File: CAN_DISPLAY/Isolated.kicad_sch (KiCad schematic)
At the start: 37 parts, among them J4 43-01199, J5 NMEA0183 Output, J7 NMEA0183 Input, J8 DCDC 5V, U3 ISO1050DUB, U4 AMS1117-5.0, U5 ISO3080DW

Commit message: Added Light Sensor
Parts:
- removed J5: NMEA0183 Output, TerminalBlock:TerminalBlock_Altech_AK300-3_P5.00mm, symbol Connector_Generic:Conn_01x03
- removed J7: NMEA0183 Input, TerminalBlock:TerminalBlock_Altech_AK300-3_P5.00mm, symbol Connector_Generic:Conn_01x03
- added J20: NMEA0183, TerminalBlock_Altech:Altech_AK300_1x06_P5.00mm_45-Degree, symbol Connector_Generic:Conn_01x06
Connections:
- net NMEA IN+: now also J20.3 (Pin_3)
- net NMEA IN-: now also J20.2 (Pin_2)
- net NMEA OUT+: now also J20.6 (Pin_6)
- net NMEA OUT-: now also J20.5 (Pin_5)
- net at JP1.1 (A): now also J20.1 (Pin_1), J20.4 (Pin_4)
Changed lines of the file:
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@@
   (junction (at 214.63 34.29) (diameter 0) (color 0 0 0 0)
   )
+  (junction (at 251.46 140.97) (diameter 0) (color 0 0 0 0)
+  )
   (junction (at 158.75 113.03) (diameter 0) (color 0 0 0 0)
   )
@@
   (junction (at 176.53 29.21) (diameter 0) (color 0 0 0 0)
   )
-  (junction (at 251.46 147.32) (diameter 0) (color 0 0 0 0)
-  )
   (junction (at 184.15 124.46) (diameter 0) (color 0 0 0 0)
   )
@@
     (stroke (width 0) (type default))
   )
+  (wire (pts (xy 246.38 135.89) (xy 254 135.89))
+    (stroke (width 0) (type default))
+  )
   (wire (pts (xy 194.31 34.29) (xy 196.85 34.29))
     (stroke (width 0) (type default))
@@
     (stroke (width 0) (type default))
   )
-  (wire (pts (xy 251.46 147.32) (xy 254 147.32))
-    (stroke (width 0) (type default))
-  )
   (wire (pts (xy 243.84 115.57) (xy 245.11 115.57))
     (stroke (width 0) (type default))
@@
     (stroke (width 0) (type default))
   )
-  (wire (pts (xy 251.46 147.32) (xy 251.46 156.21))
+  (wire (pts (xy 251.46 133.35) (xy 251.46 140.97))
     (stroke (width 0) (type default))
   )
@@
     (stroke (width 0) (type default))
   )
-  (wire (pts (xy 243.84 138.43) (xy 243.84 142.24))
-    (stroke (width 0) (type default))
-  )
   (wire (pts (xy 176.53 64.77) (xy 158.75 64.77))
     (stroke (width 0) (type default))
@@
     (stroke (width 0) (type default))
   )
+  (wire (pts (xy 248.92 140.97) (xy 248.92 138.43))
+    (stroke (width 0) (type default))
+  )
   (wire (pts (xy 205.74 21.59) (xy 205.74 24.13))
     (stroke (width 0) (type default))
@@
     (stroke (width 0) (type default))
   )
-  (wire (pts (xy 217.17 138.43) (xy 243.84 138.43))
+  (wire (pts (xy 217.17 138.43) (xy 246.38 138.43))
     (stroke (width 0) (type default))
   )
@@
     (stroke (width 0) (type default))
   )
-  (wire (pts (xy 240.03 144.78) (xy 254 144.78))
-    (stroke (width 0) (type default))
-  )
   (wire (pts (xy 153.67 66.04) (xy 168.91 66.04))
     (stroke (width 0) (type default))
@@
     (stroke (width 0) (type default))
   )
-  (wire (pts (xy 243.84 142.24) (xy 254 142.24))
-    (stroke (width 0) (type default))
-  )
-  (wire (pts (xy 214.63 140.97) (xy 240.03 140.97))
+  (wire (pts (xy 214.63 140.97) (xy 248.92 140.97))
     (stroke (width 0) (type default))
   )
@@
     (stroke (width 0) (type default))
   )
+  (wire (pts (xy 248.92 138.43) (xy 254 138.43))
+    (stroke (width 0) (type default))
+  )
   (wire (pts (xy 173.99 146.05) (xy 184.15 146.05))
     (stroke (width 0) (type default))
@@
     (stroke (width 0) (type default))
   )
-  (wire (pts (xy 240.03 140.97) (xy 240.03 144.78))
-    (stroke (width 0) (type default))
-  )
   (wire (pts (xy 226.06 50.165) (xy 226.06 52.07))
     (stroke (width 0) (type default))
@@
     (stroke (width 0) (type default))
   )
-  (wire (pts (xy 251.46 133.35) (xy 251.46 147.32))
-    (stroke (width 0) (type default))
-  )
   (wire (pts (xy 218.44 127) (xy 217.17 127))
     (stroke (width 0) (type default))
@@
     (stroke (width 0) (type default))
   )
+  (wire (pts (xy 251.46 140.97) (xy 251.46 156.21))
+    (stroke (width 0) (type default))
+  )
   (wire (pts (xy 171.45 66.04) (xy 171.45 67.945))
     (stroke (width 0) (type default))
@@
     (stroke (width 0) (type default))
   )
+  (wire (pts (xy 246.38 138.43) (xy 246.38 135.89))
+    (stroke (width 0) (type default))
+  )
   (wire (pts (xy 250.19 52.07) (xy 250.19 55.88))
     (stroke (width 0) (type default))
@@
     (stroke (width 0) (type default))
   )
+  (wire (pts (xy 251.46 140.97) (xy 254 140.97))
+    (stroke (width 0) (type default))
+  )
   (wire (pts (xy 158.75 60.96) (xy 158.75 55.88))
     (stroke (width 0) (type default))
@@
     )
   )
-  (symbol (lib_id "Connector_Generic:Conn_01x03") (at 259.08 144.78 0) (unit 1)
-    (in_bom yes) (on_board yes) (dnp no)
-    (property "Reference" "J5" (at 261.62 143.51 0)
-      (effects (font (size 1.27 1.27)) (justify left))
-    )
-    (property "Value" "NMEA0183 Output" (at 251.46 138.43 0)
-      (effects (font (size 1.27 1.27)) (justify left))
-    )
-    (property "Footprint" "TerminalBlock:TerminalBlock_Altech_AK300-3_P5.00mm" (at 259.08 144.78 0)
-      (effects (font (size 1.27 1.27)) hide)
-    )
-    (property "Datasheet" "~" (at 259.08 144.78 0)
-      (effects (font (size 1.27 1.27)) hide)
-    )
-    (pin "1")
-    (pin "2")
-    (pin "3")
-    (instances
-      (project "CAN_DISPLAY"
-        (path "/7b7bcc60-3b35-483b-8f75-db7ec854d7bb/0efeef53-f612-43e6-99d4-b53087b36e31"
-          (reference "J5") (unit 1)
-        )
-      )
-    )
-  )
   (symbol (lib_id "Device:R_Small") (at 207.01 144.78 180) (unit 1)
     (in_bom yes) (on_board yes) (dnp no)
@@
     )
   )
+  (symbol (lib_id "Connector_Generic:Conn_01x06") (at 259.08 135.89 0) (mirror x) (unit 1)
+    (in_bom yes) (on_board yes) (dnp no) (fields_autoplaced)
+    (property "Reference" "J20" (at 259.08 121.92 0)
+      (effects (font (size 1.27 1.27)))
+    )
+    (property "Value" "NMEA0183" (at 259.08 124.46 0)
+      (effects (font (size 1.27 1.27)))
+    )
+    (property "Footprint" "TerminalBlock_Altech:Altech_AK300_1x06_P5.00mm_45-Degree" (at 259.08 135.89 0)
+      (effects (font (size 1.27 1.27)) hide)
+    )
+    (property "Datasheet" "~" (at 259.08 135.89 0)
+      (effects (font (size 1.27 1.27)) hide)
+    )
+    (pin "1")
+    (pin "2")
+    (pin "3")
+    (pin "4")
+    (pin "5")
+    (pin "6")
+    (instances
+      (project "CAN_DISPLAY"
+        (path "/7b7bcc60-3b35-483b-8f75-db7ec854d7bb/0efeef53-f612-43e6-99d4-b53087b36e31"
+          (reference "J20") (unit 1)
+        )
+      )
+    )
+  )
   (symbol (lib_id "power:+5V") (at 127 105.41 0) (unit 1)
     (in_bom yes) (on_board yes) (dnp no) (fields_autoplaced)
@@
         )
       )
-    )
-  )
-  (symbol (lib_id "Connector_Generic:Conn_01x03") (at 259.08 130.81 0) (unit 1)
-    (in_bom yes) (on_board yes) (dnp no)
-    (property "Reference" "J7" (at 261.62 129.54 0)
-      (effects (font (size 1.27 1.27)) (justify left))
-    )
-    (property "Value" "NMEA0183 Input" (at 252.73 124.46 0)
-      (effects (font (size 1.27 1.27)) (justify left))
-    )
-    (property "Footprint" "TerminalBlock:TerminalBlock_Altech_AK300-3_P5.00mm" (at 259.08 130.81 0)
-      (effects (font (size 1.27 1.27)) hide)
-    )
-    (property "Datasheet" "~" (at 259.08 130.81 0)
-      (effects (font (size 1.27 1.27)) hide)
-    )
-    (pin "1")
-    (pin "2")
-    (pin "3")
-    (instances
-      (project "CAN_DISPLAY"
-        (path "/7b7bcc60-3b35-483b-8f75-db7ec854d7bb/0efeef53-f612-43e6-99d4-b53087b36e31"
-          (reference "J7") (unit 1)
-        )
-      )

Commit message: Add SW
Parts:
- J4: value 43-01199 -> NMEA2000
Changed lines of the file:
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@@
   (symbol (lib_id "1Display1:43-01199") (at 251.46 55.88 0) (unit 1)
     (in_bom yes) (on_board yes) (dnp no) (fields_autoplaced)
-    (property "Reference" "J4" (at 267.97 59.69 0)
-      (effects (font (size 1.524 1.524)) (justify left))
+    (property "Reference" "J4" (at 260.35 48.26 0)
+      (effects (font (size 1.524 1.524)))
     )
-    (property "Value" "43-01199" (at 267.97 62.23 0)
-      (effects (font (size 1.524 1.524)) (justify left))
+    (property "Value" "NMEA2000" (at 260.35 50.8 0)
+      (effects (font (size 1.524 1.524)))
     )
     (property "Footprint" "1Display1:CONN5_43-01199_Vlad" (at 261.62 69.85 0)

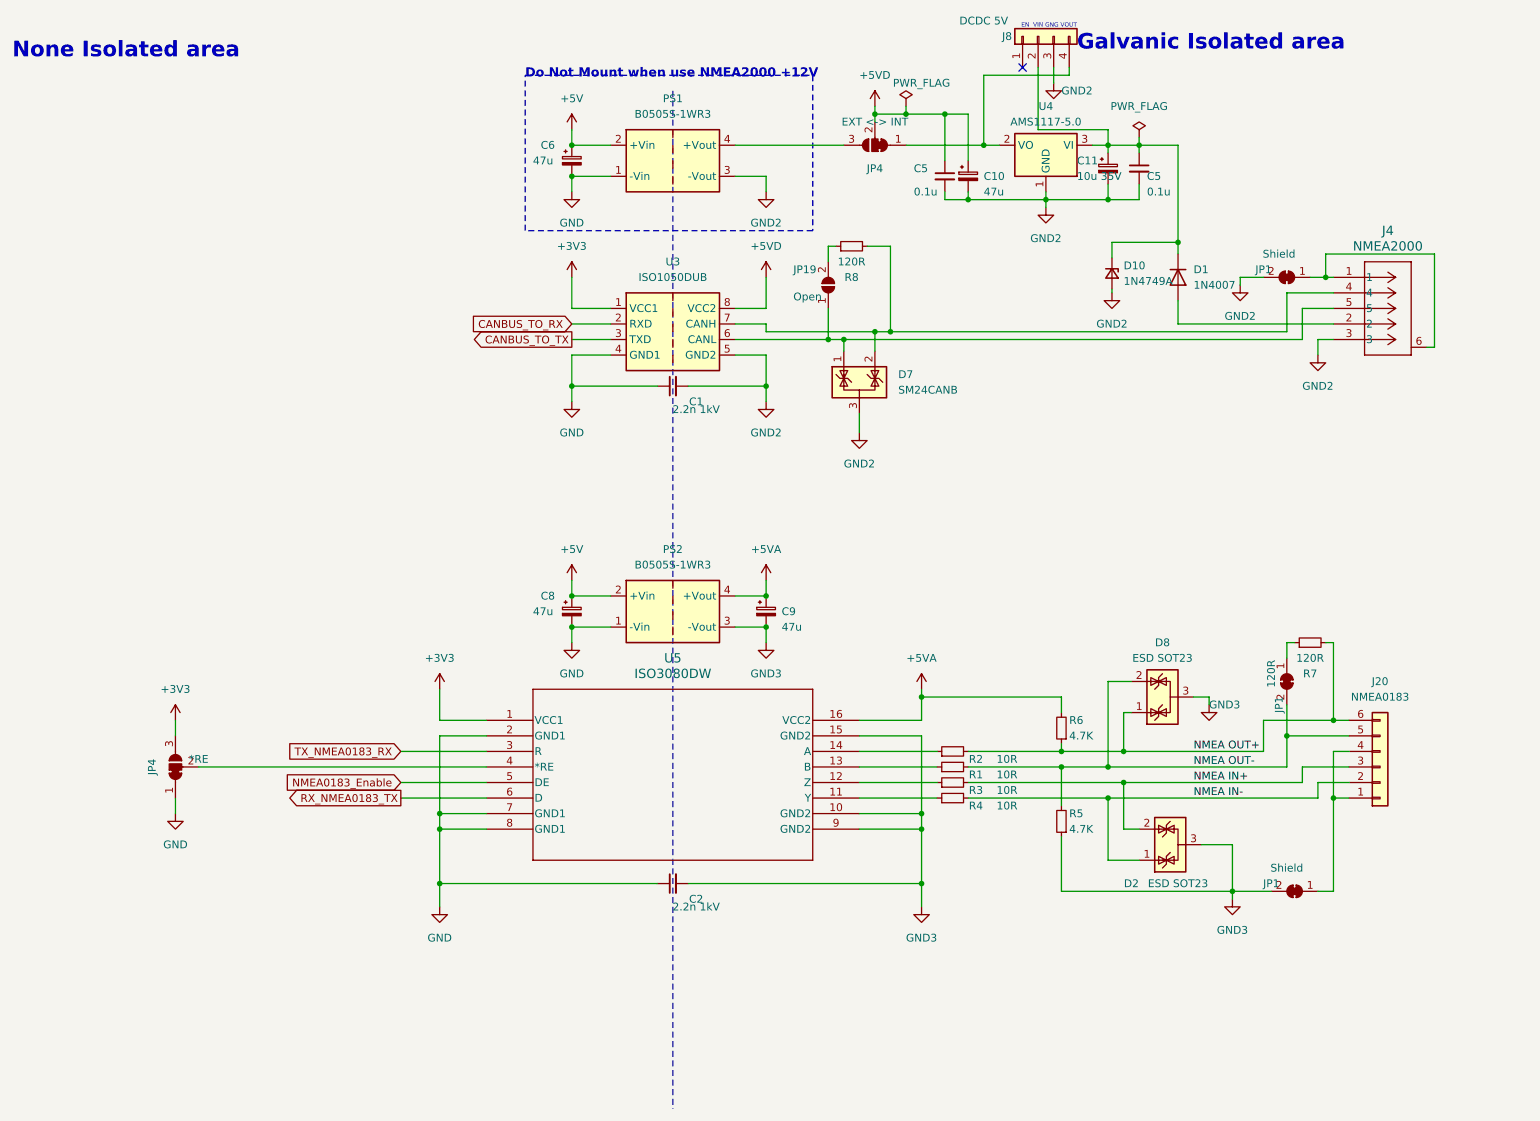
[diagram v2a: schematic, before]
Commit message: Comments CAN bus Power
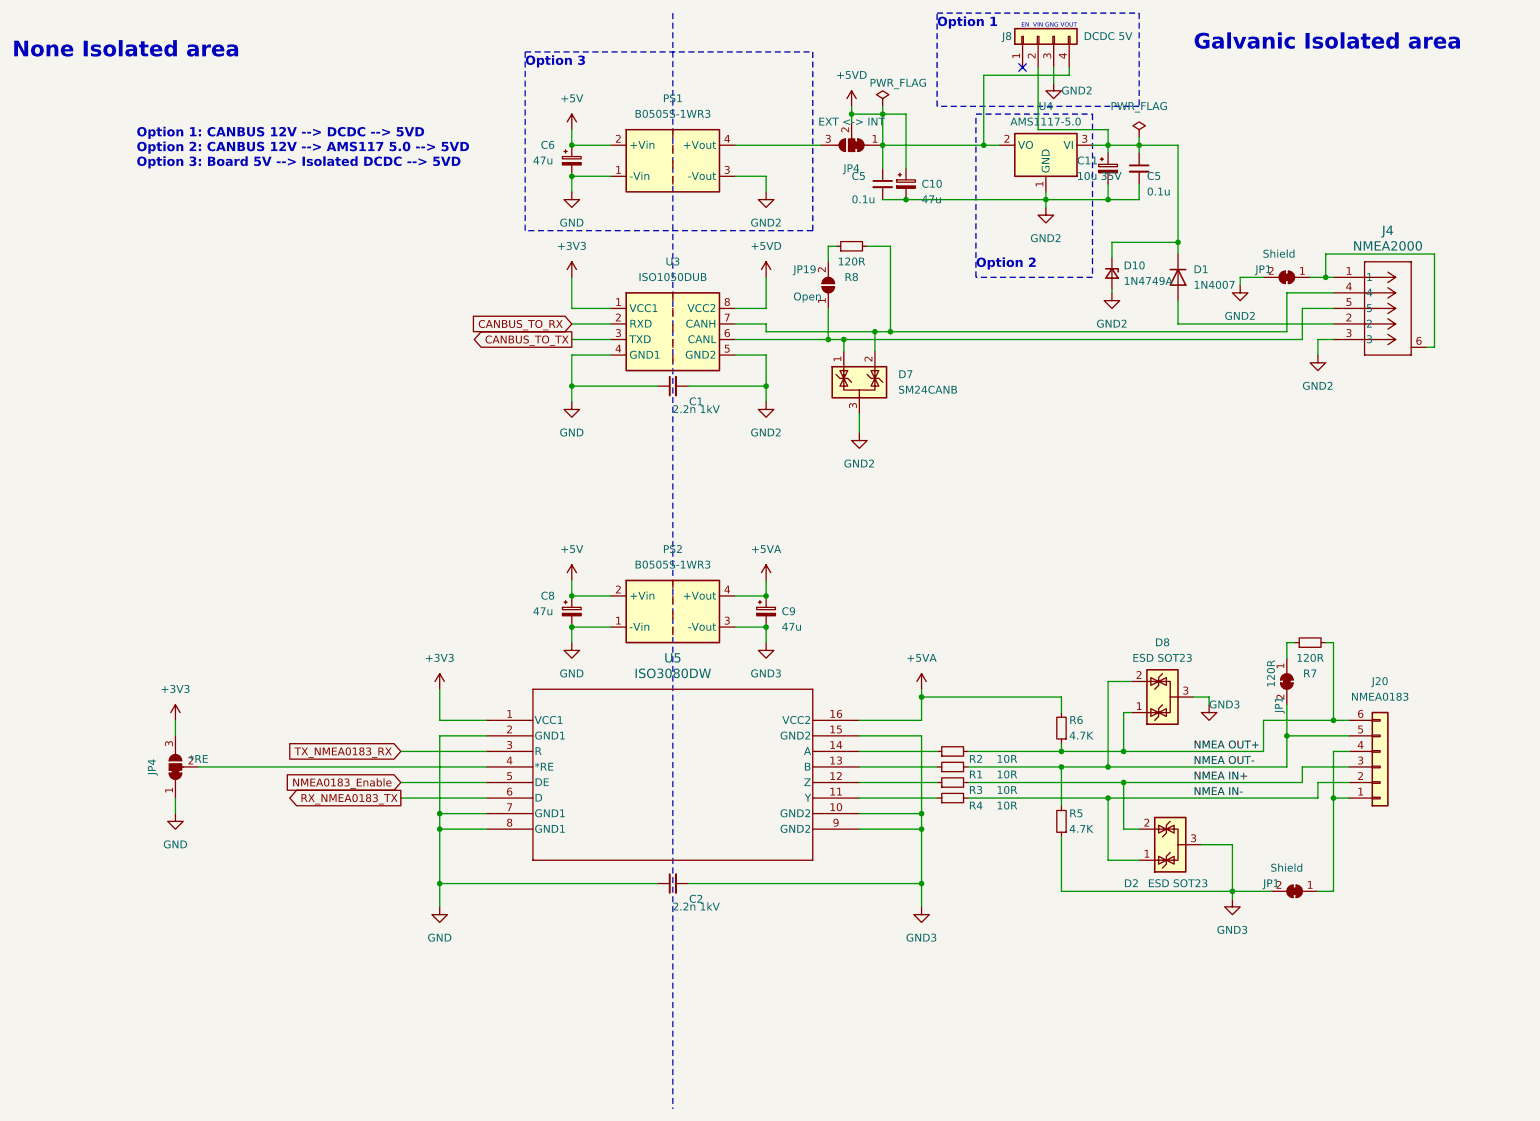
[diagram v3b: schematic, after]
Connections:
- net +5VD: now also J8.4 (Pin_4), JP4.1 (A), U4.2 (VO)
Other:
- note added: "Option 1"
- note added: "Option 1: CANBUS 12V --> DCDC --> 5VD Option 2: CANBUS 12V --> AMS117 5.0 --> 5VD Option 3: Board 5V --> Isolated DCDC --> 5VD"
- note added: "Option 2"
- note added: "Option 3"
- note removed: "Do Not Mount when use NMEA2000 +12V"
- moved on the sheet: C10, C5, JP4

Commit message: Release Version 1.00 Rev 1.00
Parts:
- added C5 (x2): 0.1u, Capacitor_SMD:C_0805_2012Metric_Pad1.18x1.45mm_HandSolder, symbol Device:C_Small
- JP4: now left out of the parts list
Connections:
- net +5V: now also C5.1
- net +5VA: now also C5.1
- net +5VD: no longer J8.4 (Pin_4), JP4.1 (A), U4.2 (VO)
- net GND: now also C5.2
- net GND3: now also C5.2
- new net: J8.4 (Pin_4), JP4.1 (A), U4.2 (VO)
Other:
- note added: "Option 1 or 2"
- moved on the sheet: C10, C5, J8, U4

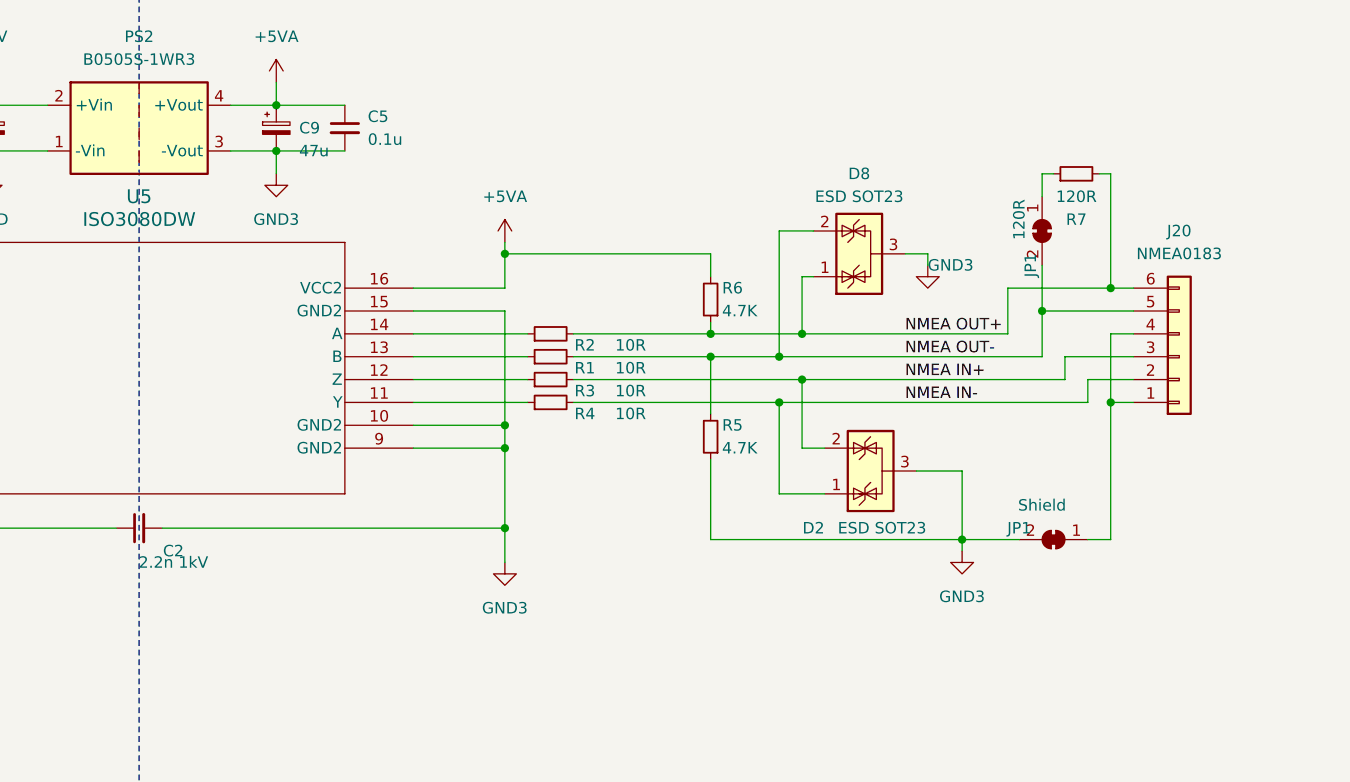
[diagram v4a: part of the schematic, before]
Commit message: Added Board Test
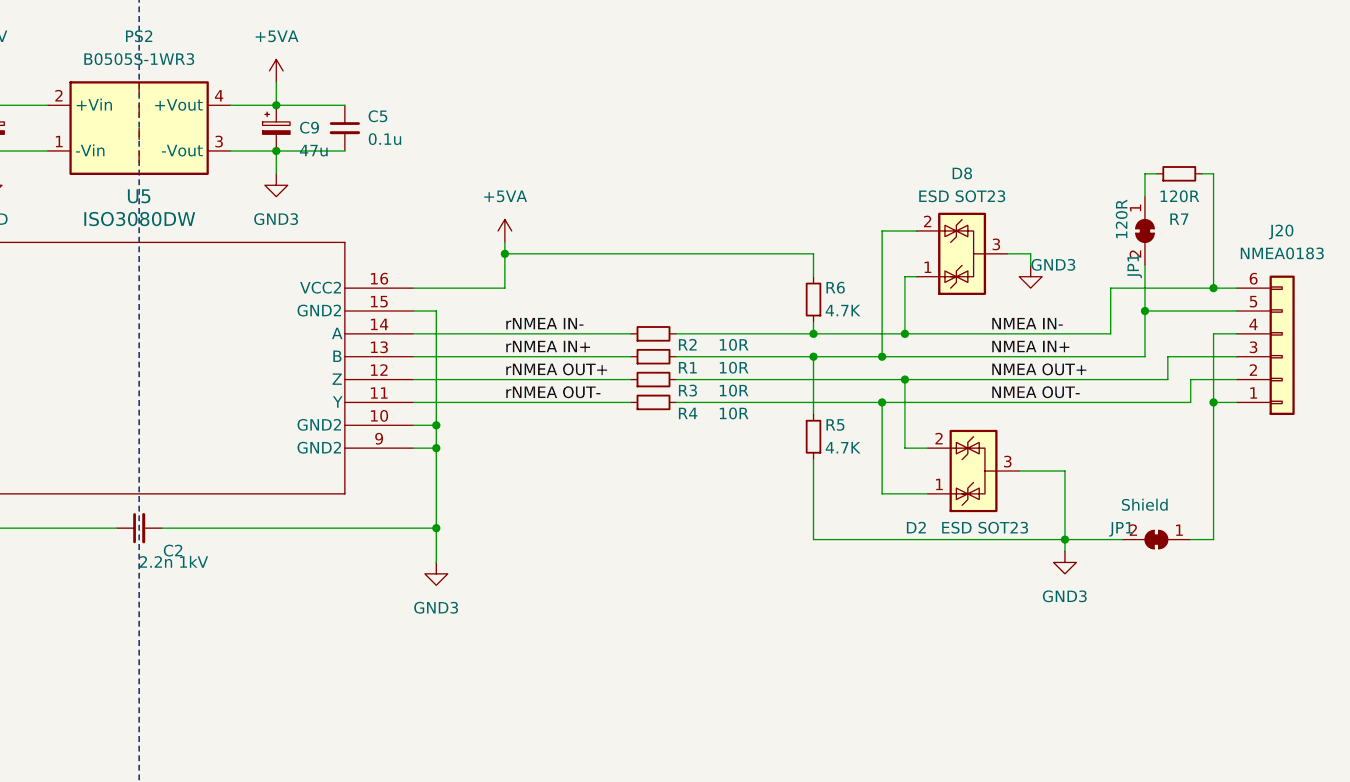
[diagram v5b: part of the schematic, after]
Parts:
- J20: footprint TerminalBlock_Altech:Altech_AK300_1x06_P5.00mm_45-Degree -> TerminalBlock:TerminalBlock_bornier-6_P5.08mm
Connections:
- net NMEA IN+: now also D8.2 (K), J20.5 (Pin_5), JP1.2 (B), R1.2, R5.2; no longer D2.2 (K), J20.3 (Pin_3), R3.2
- net NMEA IN-: now also D8.1 (K), J20.6 (Pin_6), R2.2, R6.1, R7.2; no longer D2.1 (K), J20.2 (Pin_2), R4.2
- net NMEA OUT+: now also D2.2 (K), J20.3 (Pin_3), R3.2; no longer D8.1 (K), J20.6 (Pin_6), R2.2, R6.1, R7.2
- net NMEA OUT-: now also D2.1 (K), J20.2 (Pin_2), R4.2; no longer D8.2 (K), J20.5 (Pin_5), JP1.2 (B), R1.2, R5.2
- net rNMEA IN+: now reaches R1.1, U5.13 (B)
- net rNMEA IN-: now reaches R2.1, U5.14 (A)
- net rNMEA OUT+: now reaches R3.1, U5.12 (Z)
- net rNMEA OUT-: now reaches R4.1, U5.11 (Y)
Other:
- moved on the sheet: D2, D8, J20, JP1, R1, R2, R3, R4, R5, R6, R7

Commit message: 1234
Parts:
- J20: footprint TerminalBlock:TerminalBlock_bornier-6_P5.08mm -> TerminalBlock_Altech:Altech_AK300_1x06_P5.00mm_45-Degree
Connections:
- net NMEA IN+: now also D2.2 (K), J20.3 (Pin_3), R3.2; no longer D8.2 (K), J20.5 (Pin_5), JP1.2 (B), R1.2, R5.2
- net NMEA IN-: now also D2.1 (K), J20.2 (Pin_2), R4.2; no longer D8.1 (K), J20.6 (Pin_6), R2.2, R6.1, R7.2
- net NMEA OUT+: now also D8.1 (K), J20.6 (Pin_6), R2.2, R6.1, R7.2; no longer D2.2 (K), J20.3 (Pin_3), R3.2
- net NMEA OUT-: now also D8.2 (K), J20.5 (Pin_5), JP1.2 (B), R1.2, R5.2; no longer D2.1 (K), J20.2 (Pin_2), R4.2
- net rNMEA IN+: no longer names the net of R1.1, U5.13 (B)
- net rNMEA IN-: no longer names the net of R2.1, U5.14 (A)
- net rNMEA OUT+: no longer names the net of R3.1, U5.12 (Z)
- net rNMEA OUT-: no longer names the net of R4.1, U5.11 (Y)
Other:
- moved on the sheet: D2, D8, J20, JP1, R1, R2, R3, R4, R5, R6, R7
